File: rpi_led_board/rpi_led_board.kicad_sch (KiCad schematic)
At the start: 63 parts, among them P1 Conn_02x20_Odd_Even

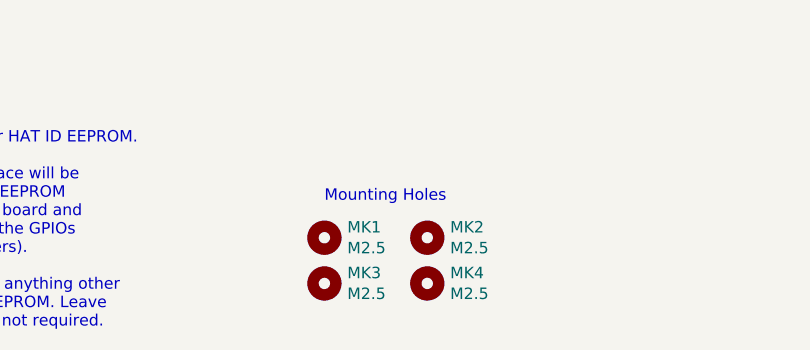
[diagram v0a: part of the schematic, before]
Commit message: updated silkscreen
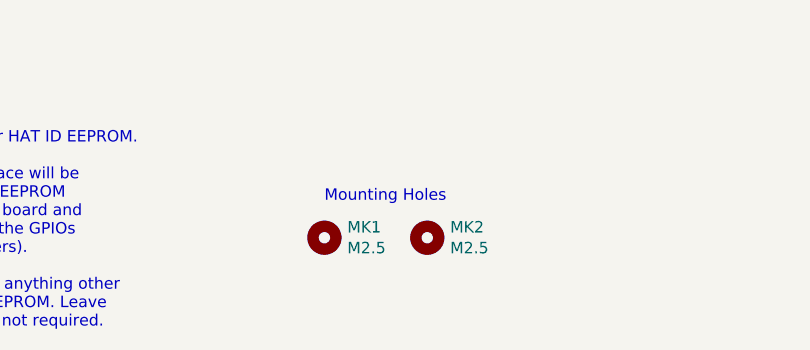
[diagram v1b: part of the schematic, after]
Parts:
- removed MK3, MK4: M2.5, MountingHole:MountingHole_2.7mm_M2.5, symbol Mechanical:MountingHole
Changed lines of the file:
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@@
-    )
-  )
-  (symbol (lib_id "Mechanical:MountingHole") (at 76.2 187.96 0) (unit 1)
-    (in_bom yes) (on_board yes)
-    (property "Reference" "MK3" (id 0) (at 78.74 186.7916 0)
-      (effects (font (size 1.27 1.27)) (justify left))
-    )
-    (property "Value" "M2.5" (id 1) (at 78.74 189.103 0)
-      (effects (font (size 1.27 1.27)) (justify left))
-    )
-    (property "Footprint" "MountingHole:MountingHole_2.7mm_M2.5" (id 2) (at 76.2 187.96 0)
-      (effects (font (size 1.524 1.524)) hide)
-    )
-    (property "Datasheet" "~" (id 3) (at 76.2 187.96 0)
-      (effects (font (size 1.524 1.524)) hide)
-    )
-  )
-  (symbol (lib_id "Mechanical:MountingHole") (at 87.63 187.96 0) (unit 1)
-    (in_bom yes) (on_board yes)
-    (property "Reference" "MK4" (id 0) (at 90.17 186.7916 0)
-      (effects (font (size 1.27 1.27)) (justify left))
-    )
-    (property "Value" "M2.5" (id 1) (at 90.17 189.103 0)
-      (effects (font (size 1.27 1.27)) (justify left))
-    )
-    (property "Footprint" "MountingHole:MountingHole_2.7mm_M2.5" (id 2) (at 87.63 187.96 0)
-      (effects (font (size 1.524 1.524)) hide)
-    )
-    (property "Datasheet" "~" (id 3) (at 87.63 187.96 0)
-      (effects (font (size 1.524 1.524)) hide)
     )
   )
@@
       (reference "MK2") (unit 1) (value "M2.5") (footprint "MountingHole:MountingHole_2.7mm_M2.5")
     )
-    (path "/00000000-0000-0000-0000-00005834fc19"
-      (reference "MK3") (unit 1) (value "M2.5") (footprint "MountingHole:MountingHole_2.7mm_M2.5")
-    )
-    (path "/00000000-0000-0000-0000-00005834fc4f"
-      (reference "MK4") (unit 1) (value "M2.5") (footprint "MountingHole:MountingHole_2.7mm_M2.5")
-    )
     (path "/00000000-0000-0000-0000-000059ad464a"
